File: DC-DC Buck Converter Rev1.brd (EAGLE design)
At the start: 115.6 x 77.5 mm, 37 parts, among them J1 APP_2POS_CONFIG5V_HORIZ, J2 APP_2POS_CONFIG5V_HORIZ, J4 APP_2POS_CONFIG12V_HORIZ, U1 OKI-78SR-5/1.5-W36HC

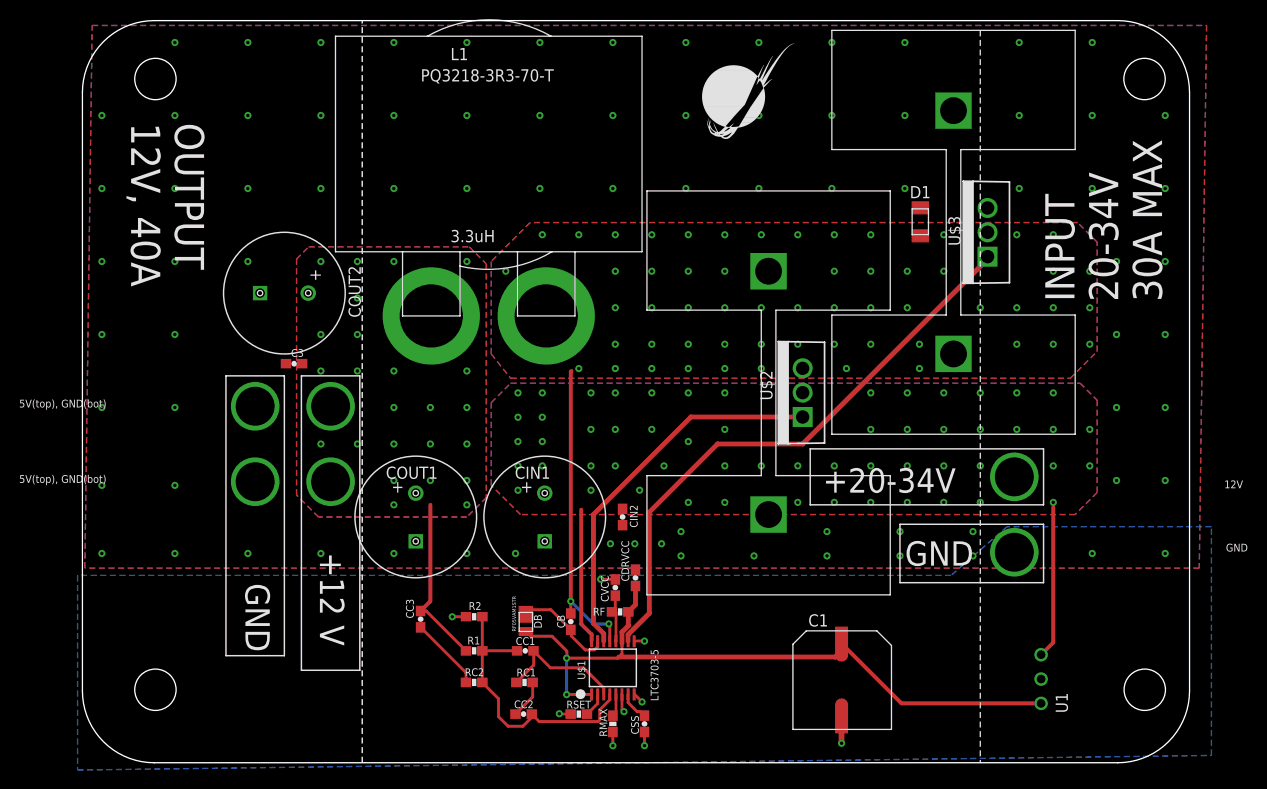
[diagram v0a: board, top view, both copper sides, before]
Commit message: Small changes
Replaced Oki capacitor, moved diode, deleted output anderson
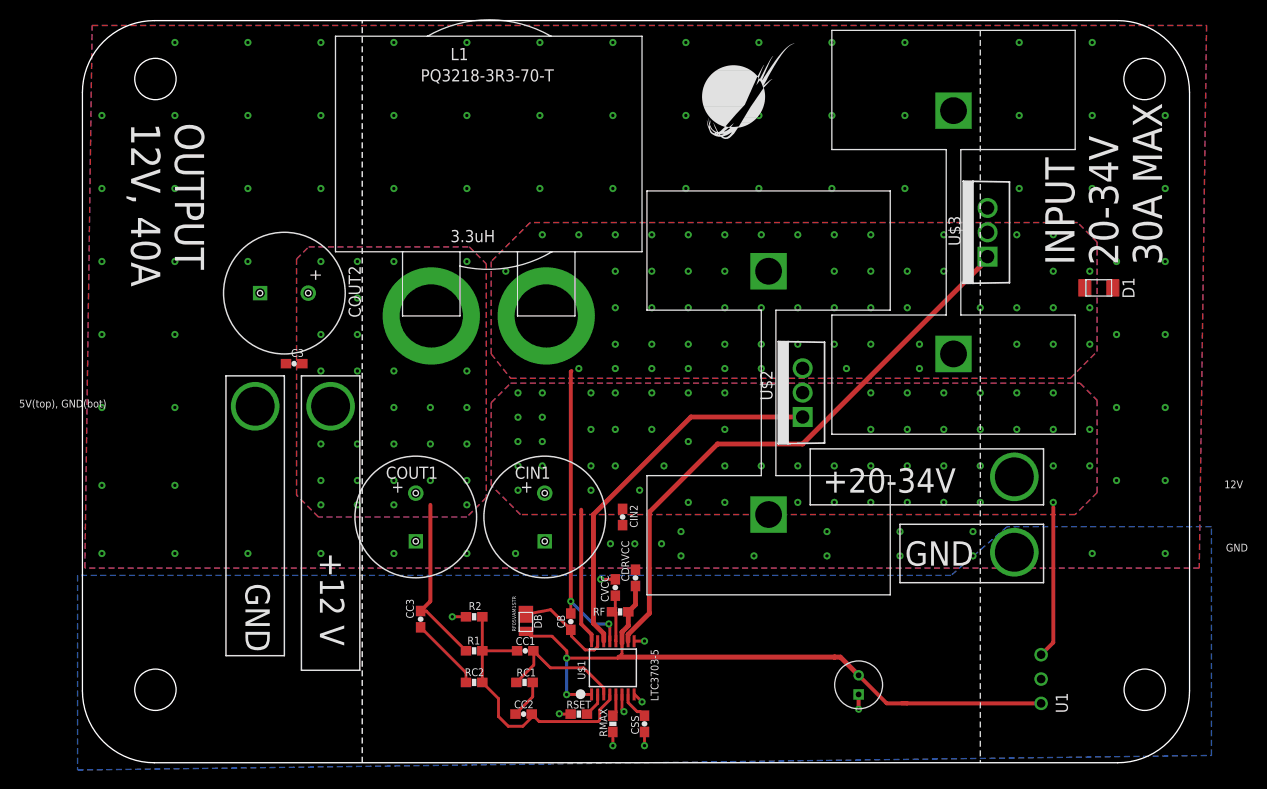
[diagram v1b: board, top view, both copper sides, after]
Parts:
- removed C1: 22u, buckconverter:CAP_POL_22UF
- removed J2: APP_2POS_CONFIG5V_HORIZ, MRDT-Connectors:APP45_5V_HORIZ_CONFIG
- added U$6: BLAH, buckconverter:BLAH
- moved D1 18.7 mm to (105.0, 49.9), turned to 270 degrees
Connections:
- net 5V: now also U$6.P$2; no longer C1.+
- net GND: now also U$6.P$1; no longer C1.-, J2.GND
- net VOUT12+: no longer J2.5V
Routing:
- net GND: track 13.9 -> 12.7 mm
- net 5V: track 73.8 -> 72.9 mm
- net VOUT12+: vias 24 -> 28
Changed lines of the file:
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@@
 <?xml version="1.0" encoding="utf-8"?>
 <!DOCTYPE eagle SYSTEM "eagle.dtd">
-<eagle version="8.3.1">
+<eagle version="8.4.1">
 <drawing>
 <settings>
@@
 <setting verticaltext="up"/>
 </settings>
-<grid distance="0.15" unitdist="inch" unit="inch" style="lines" multiple="1" display="yes" altdistance="0.001" altunitdist="inch" altunit="inch"/>
+<grid distance="0.05" unitdist="inch" unit="inch" style="lines" multiple="1" display="yes" altdistance="0.001" altunitdist="inch" altunit="inch"/>
 <layers>
 <layer number="1" name="Top" color="4" fill="1" visible="yes" active="yes"/>
@@
 <text x="5.334" y="66.294" size="3.048" layer="21" font="vector" rot="SR270">OUTPUT
 12V, 40A</text>
-<text x="112.9538" y="47.625" size="3.048" layer="21" font="vector" rot="SR90">INPUT
+<text x="112.9538" y="51.435" size="3.048" layer="21" font="vector" rot="SR90">INPUT
 20-34V
 30A MAX</text>
@@
 <param name="dpMaxLengthDifference" value="10mm"/>
 <param name="dpGapFactor" value="2.5"/>
-<param name="checkGrid" value="0"/>
 <param name="checkAngle" value="0"/>
 <param name="checkFont" value="1"/>
 <param name="checkRestrict" value="1"/>
+<param name="checkStop" value="0"/>
 <param name="useDiameter" value="13"/>
 <param name="maxErrors" value="50"/>
@@
 </autorouter>
 <elements>
-<element name="C1" library="buckconverter" package="CAP_POL_22UF" value="22u" x="79.502" y="8.128" smashed="yes">
-<attribute name="NAME" x="76.0222" y="13.716" size="1.27" layer="25" font="vector"/>
-<attribute name="VALUE" x="75.3872" y="1.397" size="1.27" layer="27" font="vector"/>
-</element>
 <element name="C3" library="SparkFun-Passives" package="0603-CAP" value="22p" x="22.352" y="41.148" smashed="yes" rot="R180">
 <attribute name="NAME" x="23.368" y="42.672" size="0.8128" layer="25" font="vector" rot="R180"/>
@@
 <attribute name="COLOR2" value="BLACK" x="-9.906" y="32.766" size="1.778" layer="27" display="off"/>
 </element>
-<element name="J2" library="MRDT-Connectors" package="APP45_5V_HORIZ_CONFIG" value="APP_2POS_CONFIG5V_HORIZ" x="-9.906" y="24.892">
-<attribute name="COLOR1" value="RED" x="-9.906" y="24.892" size="1.778" layer="27" display="off"/>
-<attribute name="COLOR2" value="BLACK" x="-9.906" y="24.892" size="1.778" layer="27" display="off"/>
-</element>
 <element name="L1" library="buckconverter" package="PLANAR_INDUCTOR_3.3UH" value="3.3uH" x="26.67" y="52.832"/>
 <element name="R1" library="SparkFun-Passives" package="0603-RES" value="113k" x="41.148" y="11.176" smashed="yes">
@@
 <attribute name="VALUE" x="60.386" y="5.9248" size="0.8128" layer="21" font="vector" ratio="10" rot="R90"/>
 </element>
-<element name="D1" library="buckconverter" package="DIODE_SCHOTTKY_30V_1A" value="RBR3MM30ATR" x="86.868" y="54.61"/>
+<element name="D1" library="buckconverter" package="DIODE_SCHOTTKY_30V_1A" value="RBR3MM30ATR" x="105.0036" y="49.911" rot="R270"/>
 <element name="DB" library="buckconverter" package="DIODE_STANDARD_100V" value="RF05VAM1STR" x="45.847" y="13.208" smashed="yes">
 <attribute name="NAME" x="48.2092" y="13.5128" size="0.8128" layer="25" font="vector" rot="R90"/>
@@
 <element name="U$4" library="buckconverter" package="RADIAL_FIN_HEATSINK" value="530002B02500G" x="91.186" y="54.864" rot="R90"/>
 <element name="U$5" library="buckconverter" package="RADIAL_FIN_HEATSINK" value="530002B02500G" x="71.882" y="38.1" rot="R90"/>
+<element name="U$6" library="buckconverter" package="BLAH" value="BLAH" x="81.28" y="7.62" rot="R90"/>
 </elements>
 <signals>
@@
 <contactref element="CIN2" pad="2"/>
 <contactref element="CIN1" pad="GND"/>
-<contactref element="C1" pad="-"/>
 <contactref element="J4" pad="GND"/>
 <polygon width="0.1524" layer="1" isolate="0.4064" thermals="no" rank="6">
@@
 <contactref element="CVCC" pad="2"/>
 <contactref element="J1" pad="GND"/>
-<contactref element="J2" pad="GND"/>
 <contactref element="U1" pad="2"/>
 <polygon width="0.3048" layer="16" isolate="0.4064">
@@
 <via x="98.044" y="59.436" extent="1-16" drill="0.35" shape="square"/>
 <via x="2.286" y="67.056" extent="1-16" drill="0.35" shape="square"/>
-<wire x1="79.502" y1="4.318" x2="79.502" y2="1.524" width="0.6096" layer="1"/>
-<via x="79.502" y="1.524" extent="1-16" drill="0.35" shape="square"/>
 <via x="2.286" y="21.336" extent="1-16" drill="0.35" shape="square"/>
 <via x="9.906" y="21.336" extent="1-16" drill="0.35" shape="square"/>
@@
 <via x="55.372" y="22.352" extent="1-16" drill="0.35" shape="square"/>
 <via x="45.466" y="21.336" extent="1-16" drill="0.35" shape="square"/>
+<contactref element="U$6" pad="P$1"/>
+<wire x1="81.28" y1="6.62" x2="81.28" y2="5.08" width="0.4064" layer="1"/>
+<via x="81.28" y="5.08" extent="1-16" drill="0.35" shape="square"/>
 </signal>
 <signal name="N$13">
@@
 <contactref element="U$1" pad="1"/>
 <contactref element="DB" pad="P$2"/>
-<contactref element="C1" pad="+"/>
 <contactref element="U1" pad="3"/>
 <wire x1="53.403" y1="6.619" x2="50.8" y2="6.619" width="0.3048" layer="1"/>
@@
 <wire x1="57.238" y1="15.24" x2="57.9882" y2="15.9902" width="0.508" layer="1"/>
 <wire x1="57.9882" y1="15.9902" x2="57.9882" y2="17.946" width="0.508" layer="1"/>
-<wire x1="78.848034375" y1="10.522034375" x2="56.242034375" y2="10.522034375" width="0.508" layer="1"/>
+<wire x1="78.74" y1="10.522034375" x2="78.848034375" y2="10.522034375" width="0.508" layer="1"/>
+<wire x1="78.74" y1="10.522034375" x2="56.242034375" y2="10.522034375" width="0.508" layer="1"/>
 <wire x1="50.822715625" y1="11.153284375" x2="50.822715625" y2="10.414" width="0.3048" layer="1"/>
-<wire x1="79.502" y1="11.176" x2="79.502" y2="11.938" width="0.508" layer="1"/>
-<wire x1="79.502" y1="11.176" x2="78.848034375" y2="10.522034375" width="0.508" layer="1"/>
 <wire x1="46.5582" y1="13.208" x2="47.0662" y2="12.7" width="0.3048" layer="1"/>
 <wire x1="47.0662" y1="12.7" x2="49.276" y2="12.7" width="0.3048" layer="1"/>
 <wire x1="49.276" y1="12.7" x2="50.822715625" y2="11.153284375" width="0.3048" layer="1"/>
-<wire x1="79.502" y1="11.938" x2="85.7504" y2="5.6896" width="0.4064" layer="1"/>
-<wire x1="85.7504" y1="5.6896" x2="100.33" y2="5.6896" width="0.4064" layer="1"/>
+<wire x1="86.36" y1="5.6896" x2="85.7504" y2="5.6896" width="0.4064" layer="1"/>
+<contactref element="U$6" pad="P$2"/>
+<wire x1="86.36" y1="5.6896" x2="100.33" y2="5.6896" width="0.4064" layer="1"/>
+<wire x1="79.377965625" y1="10.522034375" x2="81.28" y2="8.62" width="0.508" layer="1"/>
+<wire x1="79.377965625" y1="10.522034375" x2="78.74" y2="10.522034375" width="0.508" layer="1"/>
+<wire x1="81.28" y1="8.62" x2="84.2104" y2="5.6896" width="0.4064" layer="1"/>
+<wire x1="84.2104" y1="5.6896" x2="86.36" y2="5.6896" width="0.4064" layer="1"/>
 </signal>
 <signal name="N$16" class="2">
@@
 <contactref element="DB" pad="P$1"/>
 <contactref element="CB" pad="1"/>
-<wire x1="46.5582" y1="15.4686" x2="49.1372" y2="15.4686" width="0.3048" layer="1"/>
+<wire x1="46.543775" y1="14.986103125" x2="49.1372" y2="15.4686" width="0.3048" layer="1"/>
 <wire x1="51.2318" y1="13.374" x2="49.1372" y2="15.4686" width="0.3048" layer="1"/>
 <wire x1="53.67873125" y1="11.2676" x2="52.7404" y2="11.2676" width="0.3048" layer="1"/>
@@
 <contactref element="COUT2" pad="+"/>
 <contactref element="J1" pad="5V"/>
-<contactref element="J2" pad="5V"/>
 <contactref element="CC3" pad="2"/>
 <contactref element="R1" pad="1"/>
@@
 <via x="32.766" y="26.416" extent="1-16" drill="0.35"/>
 <via x="40.386" y="26.416" extent="1-16" drill="0.35"/>
+<via x="28.956" y="28.956" extent="1-16" drill="0.35"/>
+<via x="25.146" y="28.956" extent="1-16" drill="0.35"/>
+<via x="28.956" y="26.416" extent="1-16" drill="0.35"/>
+<via x="25.146" y="26.416" extent="1-16" drill="0.35"/>
 </signal>
 </signals>
